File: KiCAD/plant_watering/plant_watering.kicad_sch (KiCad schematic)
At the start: 7 parts, among them J1 Barrel_Jack, P1 USB_C_Plug_USB2.0, U2 ESP32-WROOM-32

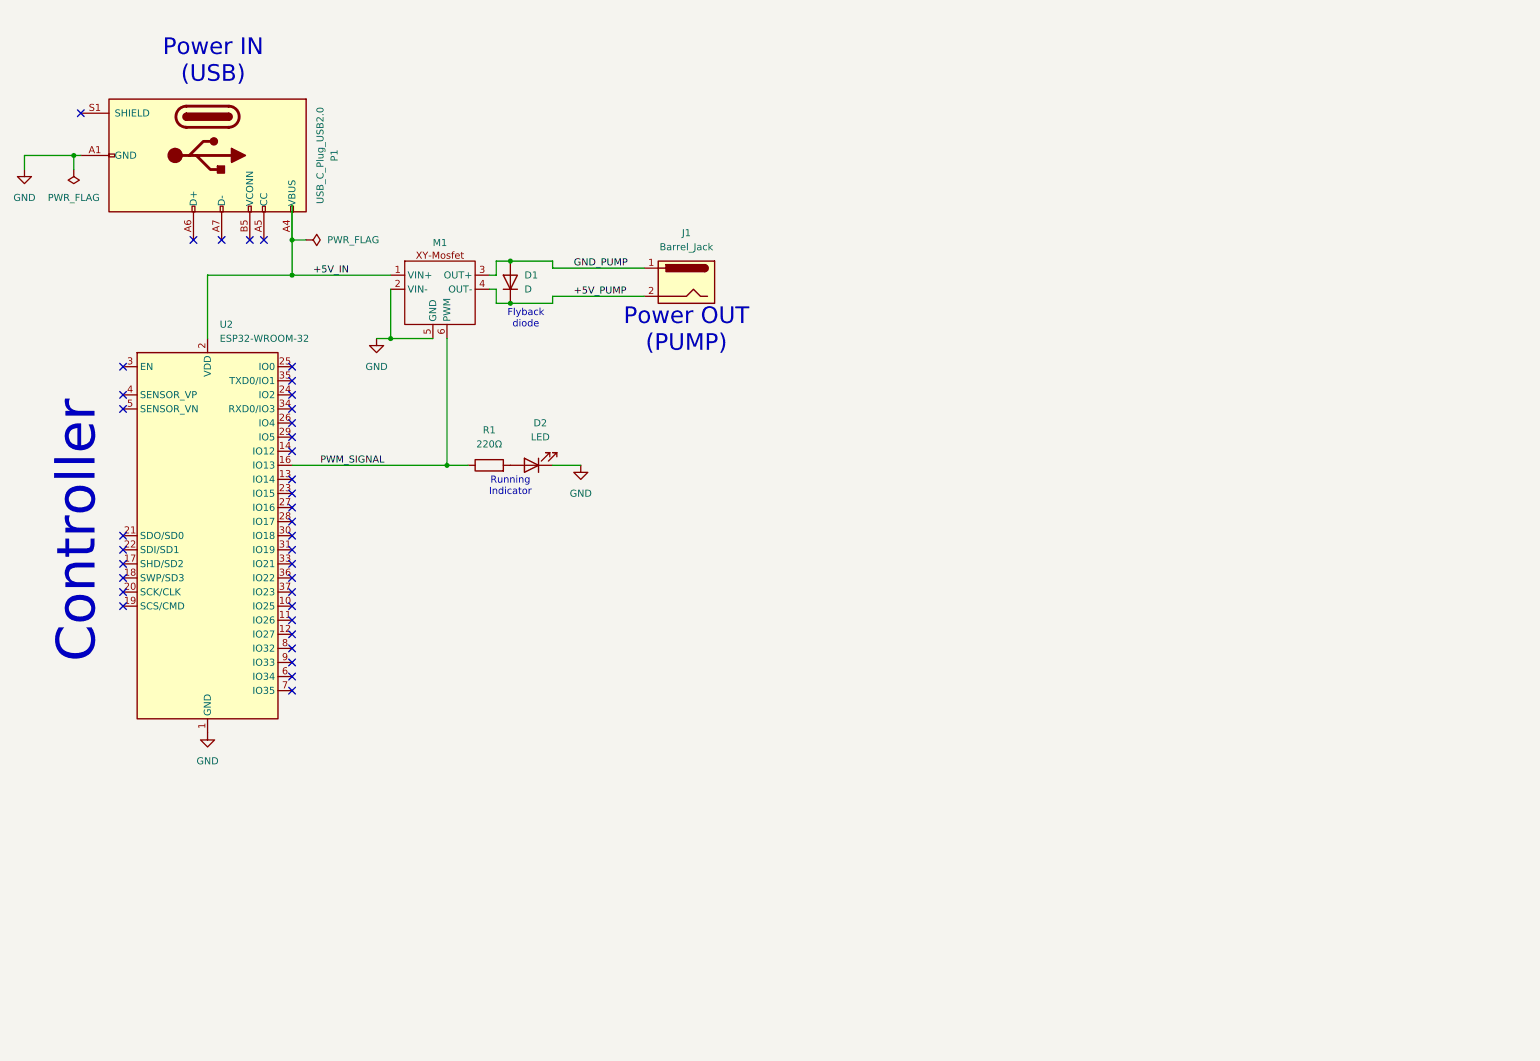
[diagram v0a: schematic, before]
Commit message: PWM working + Manual input working as well
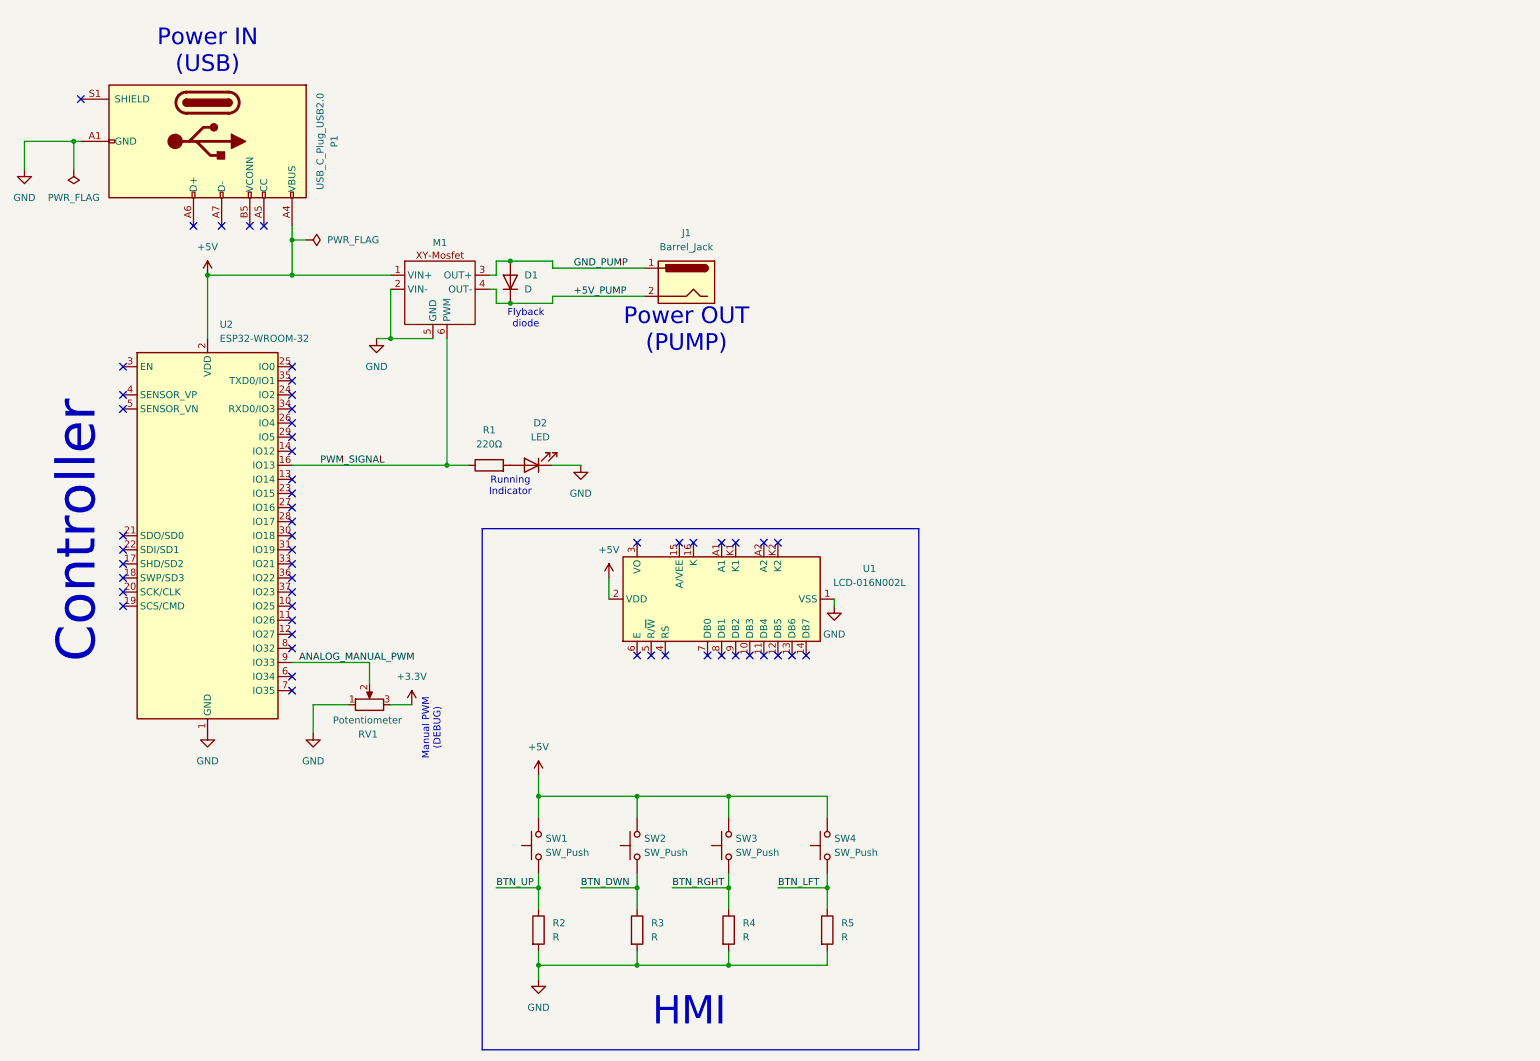
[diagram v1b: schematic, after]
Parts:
- added R2, R3, R4, R5: R, symbol Device:R
- added RV1: Potentiometer, symbol Device:R_Potentiometer
- added SW1, SW2, SW3, SW4: SW_Push, symbol Switch:SW_Push
- added U1: LCD-016N002L, Display:LCD-016N002L, symbol Display_Character:LCD-016N002L
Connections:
- net GND: now also R2.2, R3.2, R4.2, R5.2, RV1.1, U1.1 (VSS)
- net ANALOG_MANUAL_PWM: now reaches U2.9 (IO33)
- net ANALOG_MANUAL_PWM: now also RV1.2
- net +5V_IN renamed +5V
- net +5V: now also SW1.2, SW2.2, SW3.2, SW4.2, U1.2 (VDD)
- new net +3.3V: RV1.3
- new net BTN_DWN: R3.1, SW2.1
- new net BTN_LFT: R5.1, SW4.1
- new net BTN_RGHT: R4.1, SW3.1
- new net BTN_UP: R2.1, SW1.1
- no-connect marks 37 -> 54
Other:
- note added: "HMI"
- note added: "Manual PWM (DEBUG)"
- moved on the sheet: P1

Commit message: API Exchange
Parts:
- removed P1: USB_C_Plug_USB2.0, symbol Connector:USB_C_Plug_USB2.0
- removed RV1: Potentiometer, symbol Device:R_Potentiometer
- removed SW1, SW2, SW3, SW4: SW_Push, symbol Switch:SW_Push
- removed U1: LCD-016N002L, Display:LCD-016N002L, symbol Display_Character:LCD-016N002L
- removed U2: ESP32-WROOM-32, RF_Module:ESP32-WROOM-32, symbol RF_Module:ESP32-WROOM-32
- added D3, D4, D5: D, Diode_THT:D_5W_P10.16mm_Horizontal, symbol Device:D
- added D6, D7, D8: LED, LED_THT:LED_D3.0mm, symbol Device:LED
- added J10: PUMP3 PWR, Connector_JST:JST_XH_B2B-XH-A_1x02_P2.50mm_Vertical, symbol Connector_Generic:Conn_01x02
- added J11: PUMP1 PMW, Connector_JST:JST_XH_B2B-XH-A_1x02_P2.50mm_Vertical, symbol Connector_Generic:Conn_01x02
- added J12: PUMP2 PMW, Connector_JST:JST_XH_B2B-XH-A_1x02_P2.50mm_Vertical, symbol Connector_Generic:Conn_01x02
- added J13: PUMP3 PMW, Connector_JST:JST_XH_B2B-XH-A_1x02_P2.50mm_Vertical, symbol Connector_Generic:Conn_01x02
- added J2: PLANT1, Connector_JST:JST_XH_B3B-XH-A_1x03_P2.50mm_Vertical, symbol Connector_Generic:Conn_01x03
- added J3: PLANT2, Connector_JST:JST_XH_B3B-XH-A_1x03_P2.50mm_Vertical, symbol Connector_Generic:Conn_01x03
- added J4: PLANT3, Connector_JST:JST_XH_B3B-XH-A_1x03_P2.50mm_Vertical, symbol Connector_Generic:Conn_01x03
- added J5: WATER1, Connector_JST:JST_XH_B3B-XH-A_1x03_P2.50mm_Vertical, symbol Connector_Generic:Conn_01x03
- added J6: 4xLR6 1.5V Battery Pack, Connector_JST:JST_XH_B2B-XH-A_1x02_P2.50mm_Vertical, symbol Connector_Generic:Conn_01x02
- added J7: Potentiometer, Connector_JST:JST_XH_B3B-XH-A_1x03_P2.50mm_Vertical, symbol Connector_Generic:Conn_01x03
- added J8: PUMP1 PWR, Connector_JST:JST_XH_B2B-XH-A_1x02_P2.50mm_Vertical, symbol Connector_Generic:Conn_01x02
- added J9: PUMP2 PWR, Connector_JST:JST_XH_B2B-XH-A_1x02_P2.50mm_Vertical, symbol Connector_Generic:Conn_01x02
- added R6: 220Ω, Resistor_THT:R_Axial_DIN0207_L6.3mm_D2.5mm_P10.16mm_Horizontal, symbol Device:R
- added U1: ESP32-WROOM-32, Meltwin:ESP32-C3-DevKitM-1, symbol Meltwin:ESP32-WROOM-32
- D2: footprint (none) -> LED_THT:LED_D3.0mm
- R1: footprint (none) -> Resistor_THT:R_Axial_DIN0207_L6.3mm_D2.5mm_P10.16mm_Horizontal
- R2: value R -> R_Battery; footprint (none) -> Resistor_THT:R_Axial_DIN0207_L6.3mm_D2.5mm_P10.16mm_Horizontal
- R3: value R -> R_battery; footprint (none) -> Resistor_THT:R_Axial_DIN0207_L6.3mm_D2.5mm_P10.16mm_Horizontal
- R4, R5: value R -> 220Ω; footprint (none) -> Resistor_THT:R_Axial_DIN0207_L6.3mm_D2.5mm_P10.16mm_Horizontal
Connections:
- net BTN_DWN is gone; now on net GND: R3.1
- net BTN_UP is gone; now on net +6V: R2.1
- net GND: now also D6.1 (K), D7.1 (K), D8.1 (K), J10.1 (Pin_1), J11.1 (Pin_1), J12.1 (Pin_1), J13.1 (Pin_1), J2.1 (Pin_1), J3.1 (Pin_1), J4.1 (Pin_1), J5.1 (Pin_1), J6.1 (Pin_1), J7.1 (Pin_1), J8.1 (Pin_1), J9.1 (Pin_1), U1.GND; no longer R2.2, R3.2, R4.2, R5.2
- net +5V renamed +6V
- net +6V: now also J10.2 (Pin_2), J6.2 (Pin_2), J8.2 (Pin_2), J9.2 (Pin_2), U1.VIN (VDD_5V)
- net BTN_LFT renamed PUMP2_PWM
- net PUMP2_PWM: now also J12.2 (Pin_2), U1.D19 (IO19/MISO/VSPI_MISO)
- net BTN_RGHT renamed STATUS
- net STATUS: now also U1.D23 (IO23/SPI_MOSI/VSPI_MOSI)
- net PWM_SIGNAL renamed PUMP1_PWM
- net PUMP1_PWM: now also J11.2 (Pin_2), U1.D18 (IO18/SPI_SCK/VSPI_SLK)
- new net: D3.1 (K), D4.1 (K), D5.1 (K), U1.D25 (IO25/ADC2_8/DAC1)
- new net: D8.2 (A), R6.2
- new net: D6.2 (A), R4.2
- new net: D7.2 (A), R5.2
- new net +3V3: J7.3 (Pin_3), U1.3V3 (VDD_3V)
- new net BAT_LVL_3V: R2.2, R3.2, U1.D13 (IO13/ADC2_4/HSPI_MOSI/Touch4)
- new net MANUAL_PWM: J7.2 (Pin_2), U1.D4 (IO4/ADC2_0/Touch0)
- new net PLANT1_ENB: J2.3 (Pin_3), U1.D26 (IO26/ADC2_9/DAC2)
- new net PLANT1_SIG: D3.2 (A), J2.2 (Pin_2)
- new net PLANT2_ENB: J3.3 (Pin_3), U1.D27 (IO27/ADC2_7/Touch7)
- new net PLANT2_SIG: D4.2 (A), J3.2 (Pin_2)
- new net PLANT3_ENB: J4.3 (Pin_3), U1.D14 (IO14/ADC2_6/HSPI_CLK/Touch6)
- new net PLANT3_SIG: D5.2 (A), J4.2 (Pin_2)
- new net PUMP3_PWM: J13.2 (Pin_2), R6.1, U1.D21 (IO21/SDA)
- new net WATER_LEVEL_ENB: J5.3 (Pin_3), U1.D33 (IO33/ADC1_5/Touch8)
- new net WATER_LEVEL_SIG: J5.2 (Pin_2), U1.D32 (IO32/ADC1_4/Touch9)
- no-connect marks 54 -> 15
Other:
- note added: "Debug"
- note added: "Plant Sensors (Humidity)"
- note added: "Power"
- note added: "Water Level Sensor (Buffer)"
- note removed: "HMI"
- note removed: "Manual PWM (DEBUG)"
- note removed: "Power IN (USB)"
